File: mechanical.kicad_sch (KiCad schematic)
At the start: 0 parts

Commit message: added mounting holes
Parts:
- added H1, H2, H3, H4: MountingHole, MountingHole:MountingHole_6.4mm_M6, symbol Mechanical:MountingHole

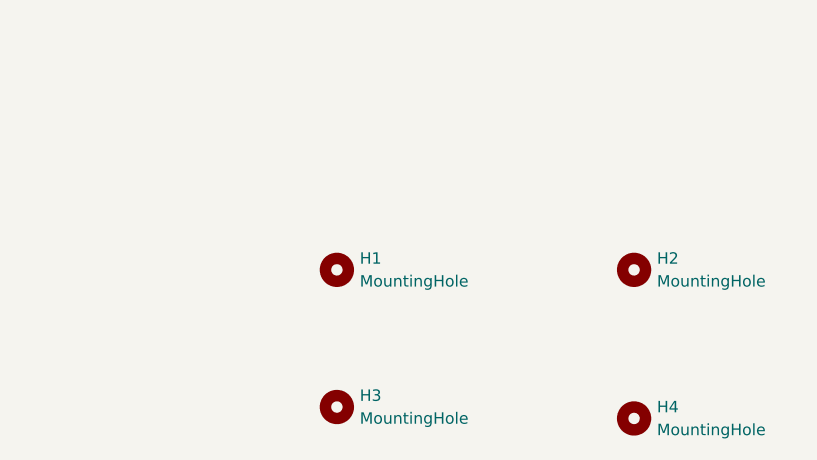
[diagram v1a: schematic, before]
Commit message: updated MCU schematic
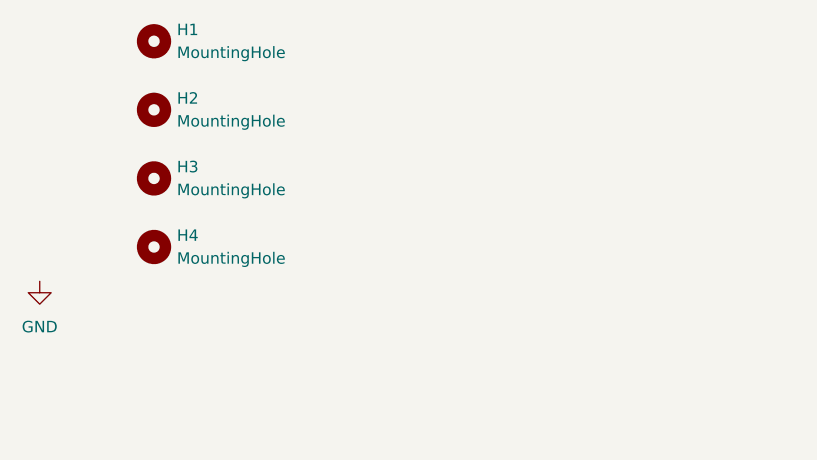
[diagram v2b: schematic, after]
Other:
- moved on the sheet: H1, H2, H3, H4
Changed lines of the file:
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@@
 	(generator "eeschema")
 	(generator_version "9.0")
-	(paper "A4")
+	(paper "A5")
 	(symbol
 		(lib_id "Mechanical:MountingHole")
-		(at 120.65 69.85 0)
+		(at 100.33 44.45 0)
 		(unit 1)
 		(exclude_from_sim no)
@@
 		(fields_autoplaced yes)
 		(property "Reference" "H1"
-			(at 123.19 68.5799 0)
+			(at 102.87 43.1799 0)
 			(effects
 				(font
@@
 		)
 		(property "Value" "MountingHole"
-			(at 123.19 71.1199 0)
+			(at 102.87 45.7199 0)
 			(effects
 				(font
@@
 		)
 		(property "Footprint" "MountingHole:MountingHole_6.4mm_M6"
-			(at 120.65 69.85 0)
+			(at 100.33 44.45 0)
 			(effects
 				(font
@@
 		)
 		(property "Datasheet" "~"
-			(at 120.65 69.85 0)
+			(at 100.33 44.45 0)
 			(effects
 				(font
@@
 		)
 		(property "Description" "Mounting Hole without connection"
-			(at 120.65 69.85 0)
+			(at 100.33 44.45 0)
 			(effects
 				(font
@@
 		)
 		(instances
-			(project ""
+			(project "Sumo_Robot"
 				(path "/f283bc71-7763-4093-b75c-cbe2f5868c12/385d545c-a594-46c7-8442-a965f8696594"
 					(reference "H1")
@@
 	(symbol
 		(lib_id "Mechanical:MountingHole")
-		(at 153.67 69.85 0)
+		(at 100.33 52.07 0)
 		(unit 1)
 		(exclude_from_sim no)
@@
 		(on_board yes)
 		(dnp no)
-		(fields_autoplaced yes)
 		(property "Reference" "H2"
-			(at 156.21 68.5799 0)
+			(at 102.87 50.7999 0)
 			(effects
 				(font
@@
 		)
 		(property "Value" "MountingHole"
-			(at 156.21 71.1199 0)
+			(at 102.87 53.3399 0)
 			(effects
 				(font
@@
 		)
 		(property "Footprint" "MountingHole:MountingHole_6.4mm_M6"
-			(at 153.67 69.85 0)
+			(at 100.33 52.07 0)
 			(effects
 				(font
@@
 		)
 		(property "Datasheet" "~"
-			(at 153.67 69.85 0)
+			(at 100.33 52.07 0)
 			(effects
 				(font
@@
 		)
 		(property "Description" "Mounting Hole without connection"
-			(at 153.67 69.85 0)
+			(at 100.33 52.07 0)
 			(effects
 				(font
@@
 		)
 		(instances
-			(project ""
+			(project "Sumo_Robot"
 				(path "/f283bc71-7763-4093-b75c-cbe2f5868c12/385d545c-a594-46c7-8442-a965f8696594"
 					(reference "H2")
@@
 	(symbol
 		(lib_id "Mechanical:MountingHole")
-		(at 153.67 86.36 0)
+		(at 100.33 67.31 0)
 		(unit 1)
 		(exclude_from_sim no)
@@
 		(fields_autoplaced yes)
 		(property "Reference" "H4"
-			(at 156.21 85.0899 0)
+			(at 102.87 66.0399 0)
 			(effects
 				(font
@@
 		)
 		(property "Value" "MountingHole"
-			(at 156.21 87.6299 0)
+			(at 102.87 68.5799 0)
 			(effects
 				(font
@@
 		)
 		(property "Footprint" "MountingHole:MountingHole_6.4mm_M6"
-			(at 153.67 86.36 0)
+			(at 100.33 67.31 0)
 			(effects
 				(font
@@
 		)
 		(property "Datasheet" "~"
-			(at 153.67 86.36 0)
+			(at 100.33 67.31 0)
 			(effects
 				(font
@@
 		)
 		(property "Description" "Mounting Hole without connection"
-			(at 153.67 86.36 0)
+			(at 100.33 67.31 0)
 			(effects
 				(font
@@
 	)
 	(symbol
+		(lib_id "power:GND")
+		(at 87.63 71.12 0)
+		(unit 1)
+		(exclude_from_sim no)
+		(in_bom yes)
+		(on_board yes)
+		(dnp no)
+		(fields_autoplaced yes)
+		(property "Reference" "#PWR057"
+			(at 87.63 77.47 0)
+			(effects
+				(font
+					(size 1.27 1.27)
+				)
+				(hide yes)
+			)
+		)
+		(property "Value" "GND"
+			(at 87.63 76.2 0)
+			(effects
+				(font
+					(size 1.27 1.27)
+				)
+			)
+		)
+		(property "Footprint" ""
+			(at 87.63 71.12 0)
+			(effects
+				(font
+					(size 1.27 1.27)
+				)
+				(hide yes)
+			)
+		)
+		(property "Datasheet" ""
+			(at 87.63 71.12 0)
+			(effects
+				(font
+					(size 1.27 1.27)
+				)
+				(hide yes)
+			)
+		)
+		(property "Description" "Power symbol creates a global label with name \"GND\" , ground"
+			(at 87.63 71.12 0)
+			(effects
+				(font
+					(size 1.27 1.27)
+				)
+				(hide yes)
+			)
+		)
+		(pin "1"
+		)
+		(instances
+			(project "Sumo_Robot"
+				(path "/f283bc71-7763-4093-b75c-cbe2f5868c12/385d545c-a594-46c7-8442-a965f8696594"
+					(reference "#PWR057")
+					(unit 1)
+				)
+			)
+		)
+	)
+	(symbol
 		(lib_id "Mechanical:MountingHole")
-		(at 120.65 85.09 0)
+		(at 100.33 59.69 0)
 		(unit 1)
 		(exclude_from_sim no)
@@
 		(fields_autoplaced yes)
 		(property "Reference" "H3"
-			(at 123.19 83.8199 0)
+			(at 102.87 58.4199 0)
 			(effects
 				(font
@@
 		)
 		(property "Value" "MountingHole"
-			(at 123.19 86.3599 0)
+			(at 102.87 60.9599 0)
 			(effects
 				(font
@@
 		)
 		(property "Footprint" "MountingHole:MountingHole_6.4mm_M6"
-			(at 120.65 85.09 0)
+			(at 100.33 59.69 0)
 			(effects
 				(font
@@
 		)
 		(property "Datasheet" "~"
-			(at 120.65 85.09 0)
+			(at 100.33 59.69 0)
 			(effects
 				(font
@@
 		)
 		(property "Description" "Mounting Hole without connection"
-			(at 120.65 85.09 0)
-			(effects
-				(font
+			(at 100.33 59.69 0)
+			(effects
+				(font
